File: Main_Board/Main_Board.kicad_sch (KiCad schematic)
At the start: 6 parts, among them U1 OKI-78SR-5_1.5-W36-C, U2 Teensy4.1_DEV-16771

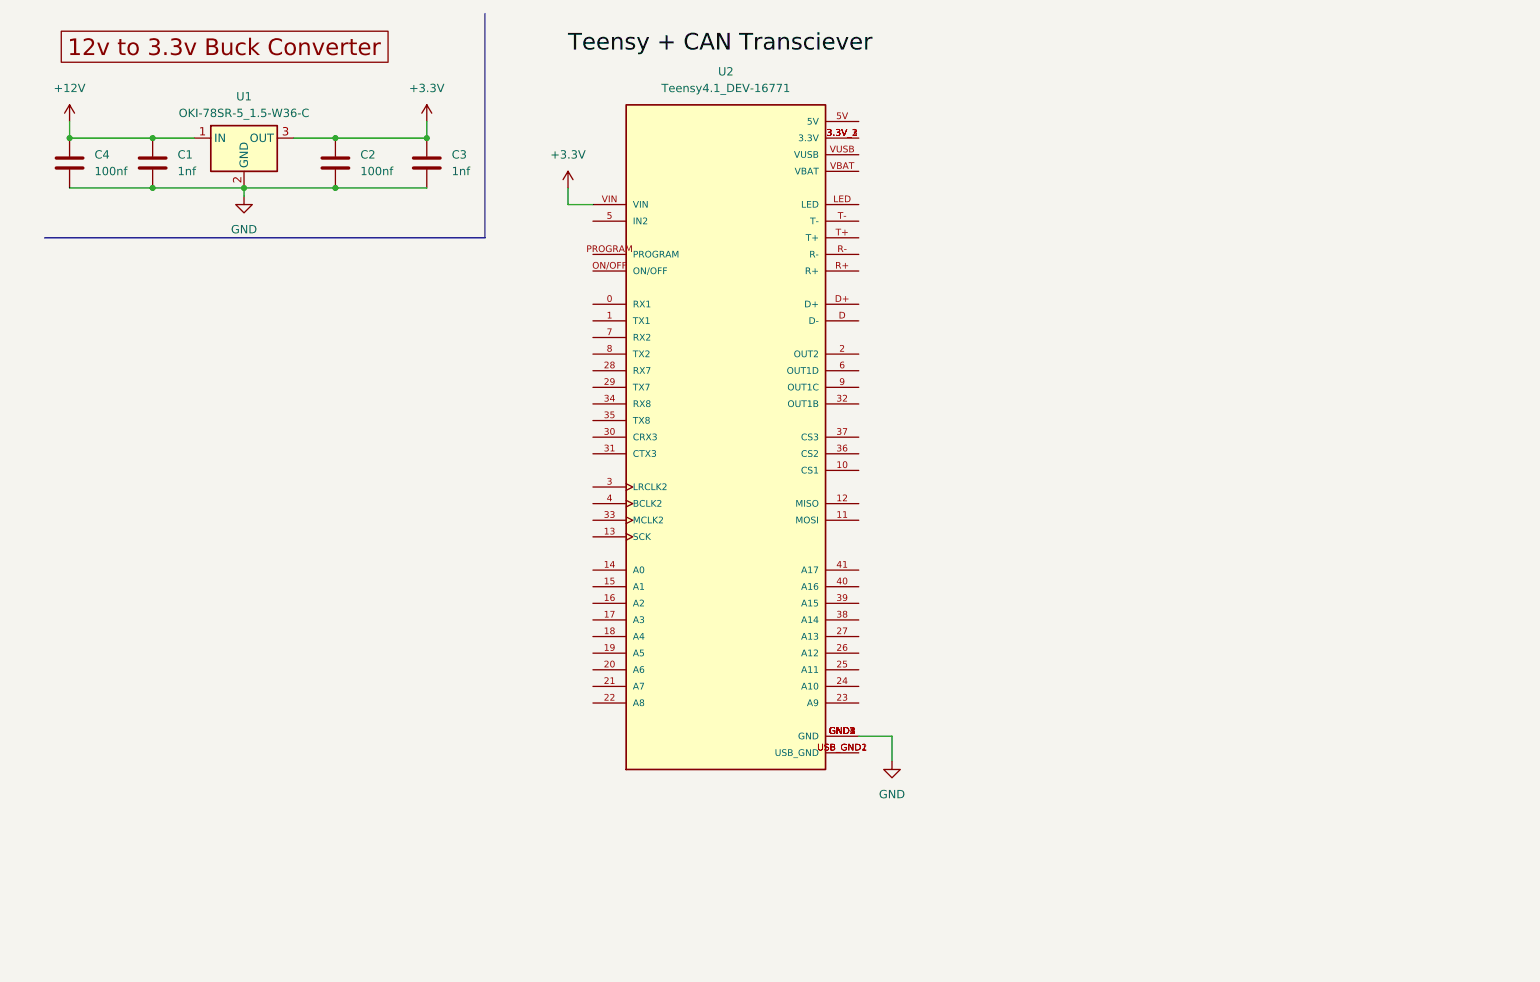
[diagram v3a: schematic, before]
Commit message: Added a Basic Can Transceiver
Added outputs and inputs to a can transceiver
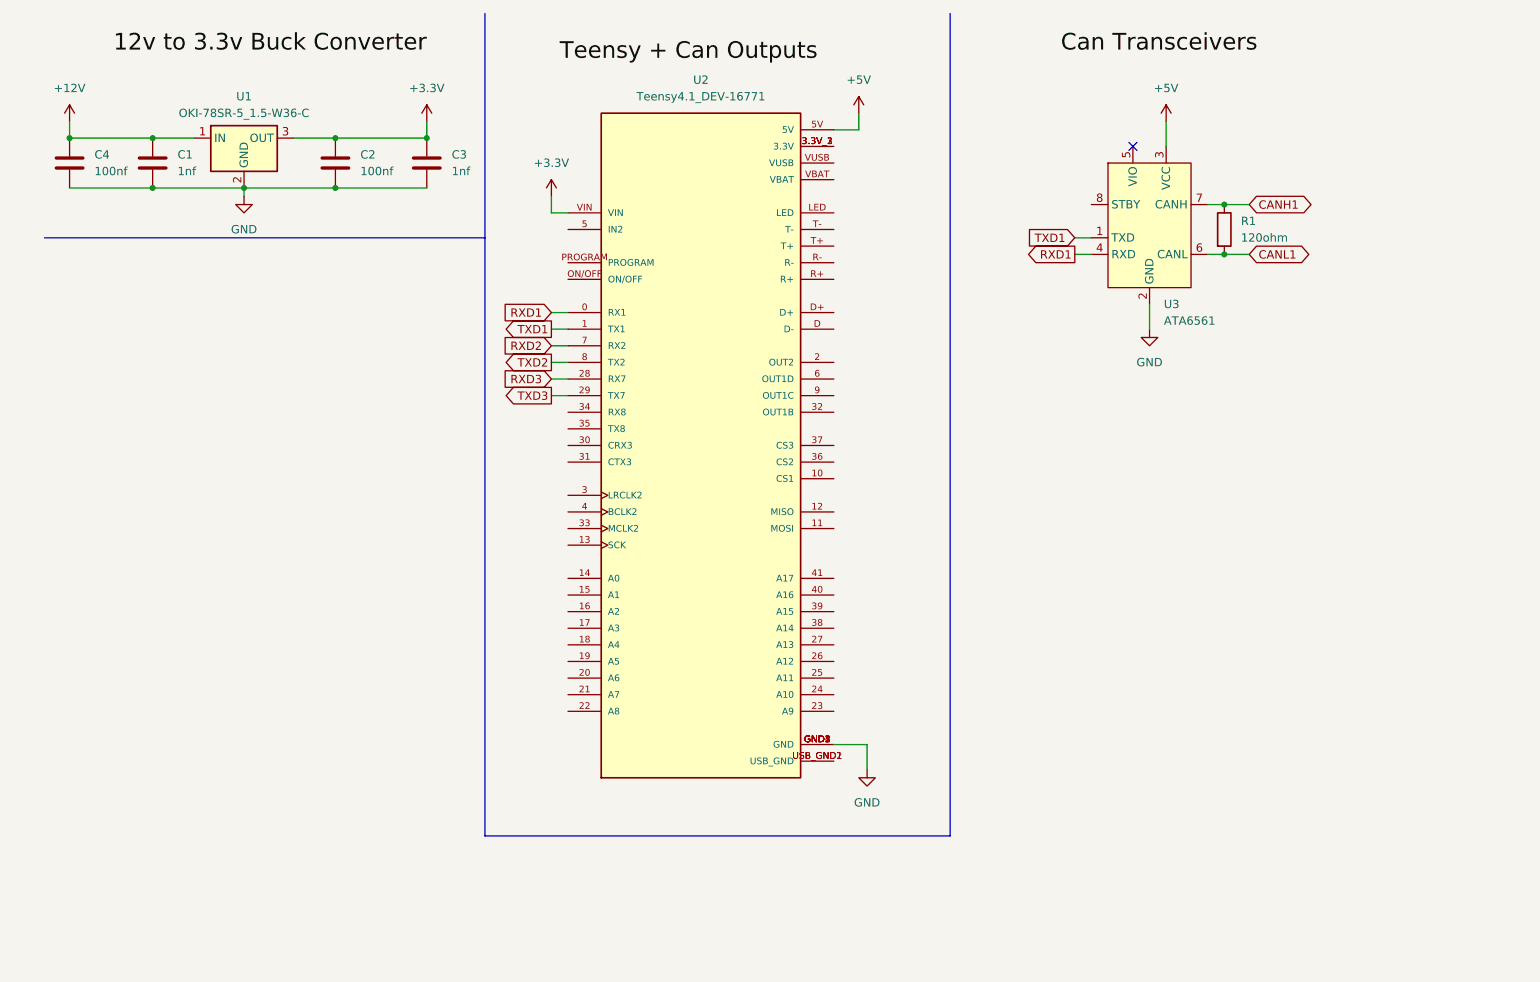
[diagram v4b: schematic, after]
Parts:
- added R1: 120ohm, symbol Device:R
- added U3: ATA6561, Package_SO:SOIC-8_3.9x4.9mm_P1.27mm, symbol MRDT_Devices:ATA6561
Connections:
- net GND: now also U3.2 (GND)
- net RXD1: now reaches U2.0 (RX1)
- net RXD1: now also U3.4 (RXD)
- net TXD1: now reaches U2.1 (TX1)
- net TXD1: now also U3.1 (TXD)
- net RXD3: now reaches U2.28 (RX7)
- net TXD3: now reaches U2.29 (TX7)
- net +5V: now reaches U2.5V
- net +5V: now also U3.3 (VCC)
- net RXD2: now reaches U2.7 (RX2)
- net TXD2: now reaches U2.8 (TX2)
- new net CANH1: R1.1, U3.7 (CANH)
- new net CANL1: R1.2, U3.6 (CANL)
- no-connect marks 0 -> 1
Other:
- moved on the sheet: U2
